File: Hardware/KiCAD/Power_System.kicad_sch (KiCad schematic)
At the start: 0 parts

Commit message: feat: add models, correct hierarchical patterns
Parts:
- added J3: USB_C_Receptacle, Connector_USB:USB_C_Receptacle_GCT_USB4085, symbol Connector:USB_C_Receptacle
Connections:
- new net: J3.A1 (GND), J3.A12 (GND), J3.B1 (GND), J3.B12 (GND)
- new net: J3.A4 (VBUS), J3.A9 (VBUS), J3.B4 (VBUS), J3.B9 (VBUS)
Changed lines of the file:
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@@
 (kicad_sch (version 20230121) (generator eeschema)
   (paper "A4")
+  (symbol (lib_id "Connector:USB_C_Receptacle") (at 46.99 87.63 0) (unit 1)
+    (in_bom yes) (on_board yes) (dnp no) (fields_autoplaced)
+    (property "Reference" "J3" (at 46.99 54.61 0)
+      (effects (font (size 1.27 1.27)))
+    )
+    (property "Value" "USB_C_Receptacle" (at 46.99 57.15 0)
+      (effects (font (size 1.27 1.27)))
+    )
+    (property "Footprint" "Connector_USB:USB_C_Receptacle_GCT_USB4085" (at 50.8 87.63 0)
+      (effects (font (size 1.27 1.27)) hide)
+    )
+    (property "Datasheet" "https://www.usb.org/sites/default/files/documents/usb_type-c.zip" (at 50.8 87.63 0)
+      (effects (font (size 1.27 1.27)) hide)
+    )
+    (pin "A1")
+    (pin "A10")
+    (pin "A11")
+    (pin "A12")
+    (pin "A2")
+    (pin "A3")
+    (pin "A4")
+    (pin "A5")
+    (pin "A6")
+    (pin "A7")
+    (pin "A8")
+    (pin "A9")
+    (pin "B1")
+    (pin "B10")
+    (pin "B11")
+    (pin "B12")
+    (pin "B2")
+    (pin "B3")
+    (pin "B4")
+    (pin "B5")
+    (pin "B6")
+    (pin "B7")
+    (pin "B8")
+    (pin "B9")
+    (pin "S1")
+    (instances
+      (project "Cobalt-Cowboy"
+        (path "/60a68eb1-aa0f-414e-b03b-965ad6b52dab/f41c6f3a-9e23-419e-9eda-91d37d832739"
+          (reference "J3") (unit 1)
+        )
+      )
+    )
+  )
 )

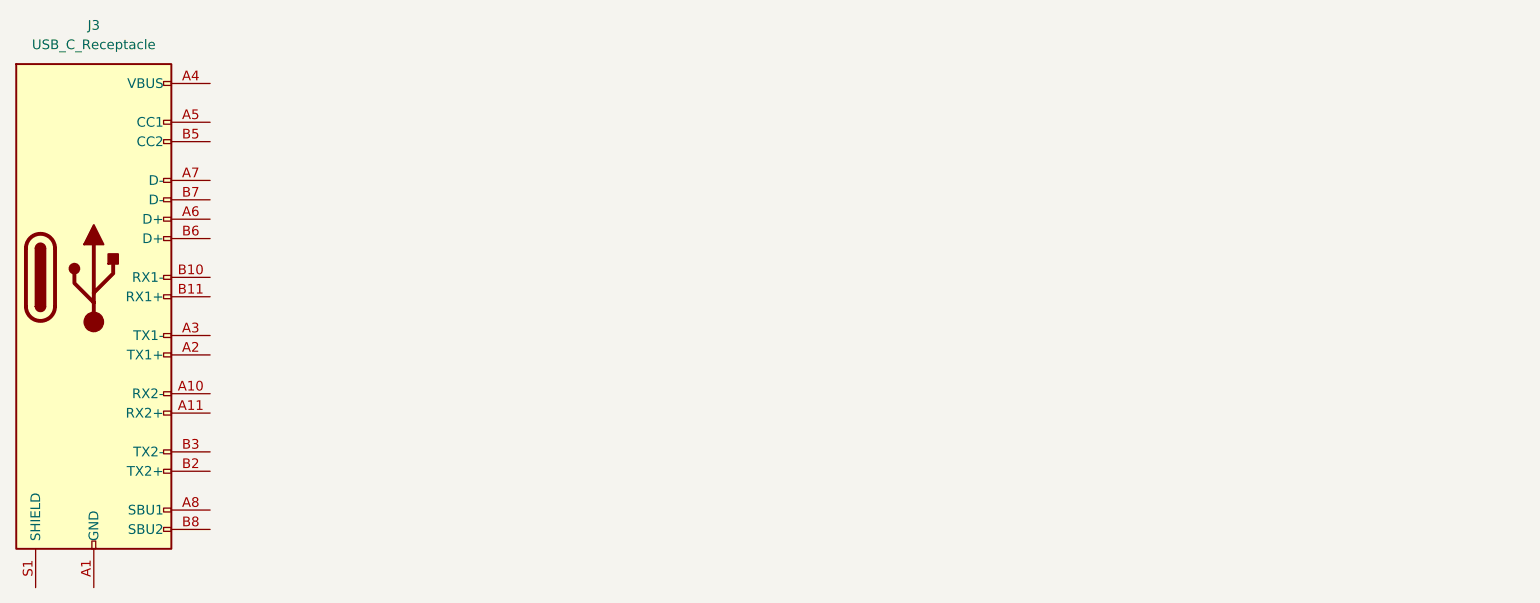
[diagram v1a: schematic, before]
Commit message: added battery to start power systen
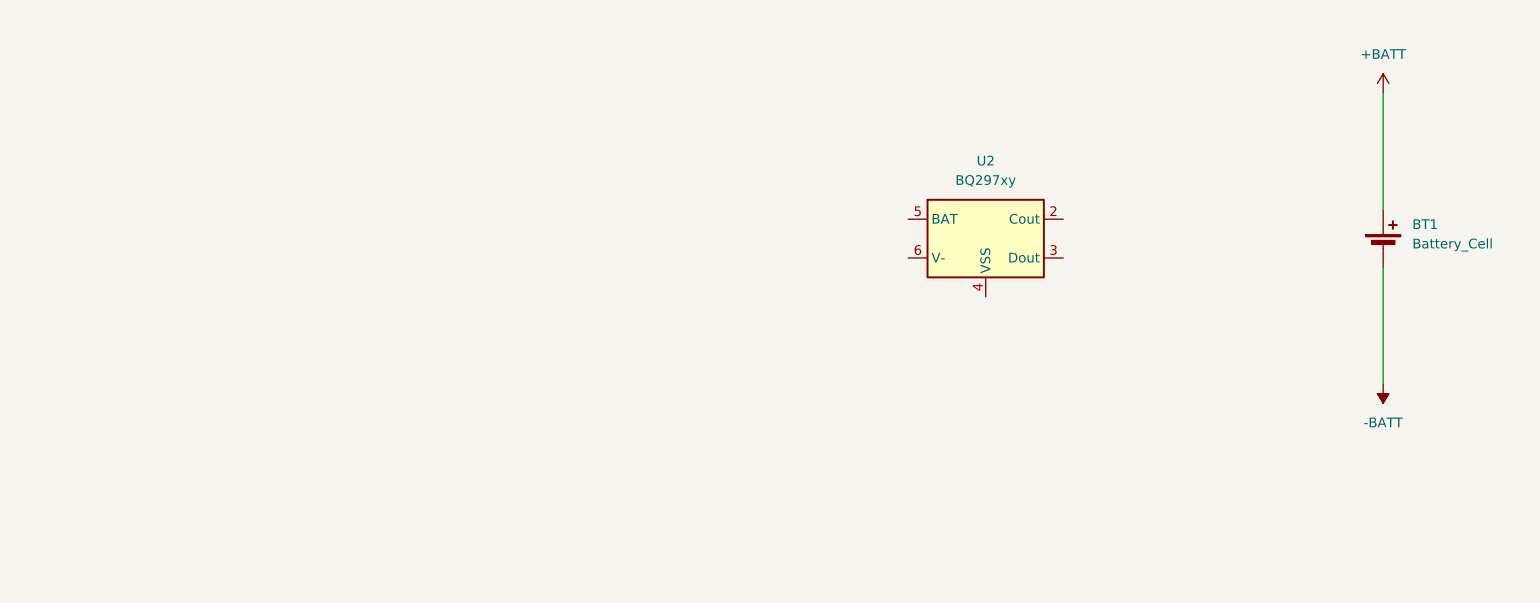
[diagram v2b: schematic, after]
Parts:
- removed J3: USB_C_Receptacle, Connector_USB:USB_C_Receptacle_GCT_USB4085, symbol Connector:USB_C_Receptacle
- added BT1: Battery_Cell, symbol Device:Battery_Cell
- added U2: BQ297xy, Package_SON:WSON-6_1.5x1.5mm_P0.5mm, symbol Battery_Management:BQ297xy
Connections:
- new net +BATT: BT1.1 (+)
- new net -BATT: BT1.2 (-)
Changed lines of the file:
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@@
 (kicad_sch (version 20230121) (generator eeschema)
   (paper "A4")
-  (symbol (lib_id "Connector:USB_C_Receptacle") (at 46.99 87.63 0) (unit 1)
+  (wire (pts (xy 215.9 63.5) (xy 215.9 78.74))
+    (stroke (width 0) (type default))
+  )
+  (wire (pts (xy 215.9 86.36) (xy 215.9 101.6))
+    (stroke (width 0) (type default))
+  )
+  (symbol (lib_id "Device:Battery_Cell") (at 215.9 83.82 0) (unit 1)
     (in_bom yes) (on_board yes) (dnp no) (fields_autoplaced)
-    (property "Reference" "J3" (at 46.99 54.61 0)
-      (effects (font (size 1.27 1.27)))
+    (property "Reference" "BT1" (at 219.71 80.7085 0)
+      (effects (font (size 1.27 1.27)) (justify left))
     )
-    (property "Value" "USB_C_Receptacle" (at 46.99 57.15 0)
-      (effects (font (size 1.27 1.27)))
+    (property "Value" "Battery_Cell" (at 219.71 83.2485 0)
+      (effects (font (size 1.27 1.27)) (justify left))
     )
-    (property "Footprint" "Connector_USB:USB_C_Receptacle_GCT_USB4085" (at 50.8 87.63 0)
+    (property "Footprint" "" (at 215.9 82.296 90)
       (effects (font (size 1.27 1.27)) hide)
     )
-    (property "Datasheet" "https://www.usb.org/sites/default/files/documents/usb_type-c.zip" (at 50.8 87.63 0)
+    (property "Datasheet" "~" (at 215.9 82.296 90)
       (effects (font (size 1.27 1.27)) hide)
     )
-    (pin "A1")
-    (pin "A10")
-    (pin "A11")
-    (pin "A12")
-    (pin "A2")
-    (pin "A3")
-    (pin "A4")
-    (pin "A5")
-    (pin "A6")
-    (pin "A7")
-    (pin "A8")
-    (pin "A9")
-    (pin "B1")
-    (pin "B10")
-    (pin "B11")
-    (pin "B12")
-    (pin "B2")
-    (pin "B3")
-    (pin "B4")
-    (pin "B5")
-    (pin "B6")
-    (pin "B7")
-    (pin "B8")
-    (pin "B9")
-    (pin "S1")
+    (pin "1")
+    (pin "2")
     (instances
       (project "Cobalt-Cowboy"
         (path "/60a68eb1-aa0f-414e-b03b-965ad6b52dab/f41c6f3a-9e23-419e-9eda-91d37d832739"
-          (reference "J3") (unit 1)
+          (reference "BT1") (unit 1)
         )
       )
+    )
+  )
+  (symbol (lib_id "Battery_Management:BQ297xy") (at 163.83 82.55 0) (unit 1)
+    (in_bom yes) (on_board yes) (dnp no) (fields_autoplaced)
+    (property "Reference" "U2" (at 163.83 72.39 0)
+      (effects (font (size 1.27 1.27)))
+    )
+    (property "Value" "BQ297xy" (at 163.83 74.93 0)
+      (effects (font (size 1.27 1.27)))
+    )
+    (property "Footprint" "Package_SON:WSON-6_1.5x1.5mm_P0.5mm" (at 163.83 73.66 0)
+      (effects (font (size 1.27 1.27)) hide)
+    )
+    (property "Datasheet" "http://www.ti.com/lit/ds/symlink/bq2970.pdf" (at 157.48 77.47 0)
+      (effects (font (size 1.27 1.27)) hide)
+    )
+    (pin "1")
+    (pin "2")
+    (pin "3")
+    (pin "4")
+    (pin "5")
+    (pin "6")
+    (instances
+      (project "Cobalt-Cowboy"
+        (path "/60a68eb1-aa0f-414e-b03b-965ad6b52dab/f41c6f3a-9e23-419e-9eda-91d37d832739"
+          (reference "U2") (unit 1)
+        )
+      )
+    )
+  )
+  (symbol (lib_id "power:-BATT") (at 215.9 101.6 180) (unit 1)
+    (in_bom yes) (on_board yes) (dnp no) (fields_autoplaced)
+    (property "Reference" "#PWR039" (at 215.9 97.79 0)
+      (effects (font (size 1.27 1.27)) hide)
+    )
+    (property "Value" "-BATT" (at 215.9 106.68 0)
+      (effects (font (size 1.27 1.27)))
+    )
+    (property "Footprint" "" (at 215.9 101.6 0)
+      (effects (font (size 1.27 1.27)) hide)
+    )
+    (property "Datasheet" "" (at 215.9 101.6 0)
+      (effects (font (size 1.27 1.27)) hide)
+    )
+    (pin "1")
+    (instances
+      (project "Cobalt-Cowboy"
+        (path "/60a68eb1-aa0f-414e-b03b-965ad6b52dab/f41c6f3a-9e23-419e-9eda-91d37d832739"
+          (reference "#PWR039") (unit 1)
+        )
+      )
+    )
+  )
+  (symbol (lib_id "power:+BATT") (at 215.9 63.5 0) (unit 1)
+    (in_bom yes) (on_board yes) (dnp no) (fields_autoplaced)
+    (property "Reference" "#PWR040" (at 215.9 67.31 0)
+      (effects (font (size 1.27 1.27)) hide)
+    )
+    (property "Value" "+BATT" (at 215.9 58.42 0)
+      (effects (font (size 1.27 1.27)))
+    )
+    (property "Footprint" "" (at 215.9 63.5 0)
+      (effects (font (size 1.27 1.27)) hide)
+    )
+    (property "Datasheet" "" (at 215.9 63.5 0)
+      (effects (font (size 1.27 1.27)) hide)
+    )
+    (pin "1")
+    (instances
+      (project "Cobalt-Cowboy"
+        (path "/60a68eb1-aa0f-414e-b03b-965ad6b52dab/f41c6f3a-9e23-419e-9eda-91d37d832739"
+          (reference "#PWR040") (unit 1)
+        )
+      )

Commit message: Added a test for commit
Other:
- note added: "Need to Add USB charging"
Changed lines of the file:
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@@
     (stroke (width 0) (type default))
+  )
+  (text "Need to Add USB charging\n" (at 13.97 16.51 0)
+    (effects (font (size 1.27 1.27)) (justify left bottom))
   )
   (symbol (lib_id "Device:Battery_Cell") (at 215.9 83.82 0) (unit 1)

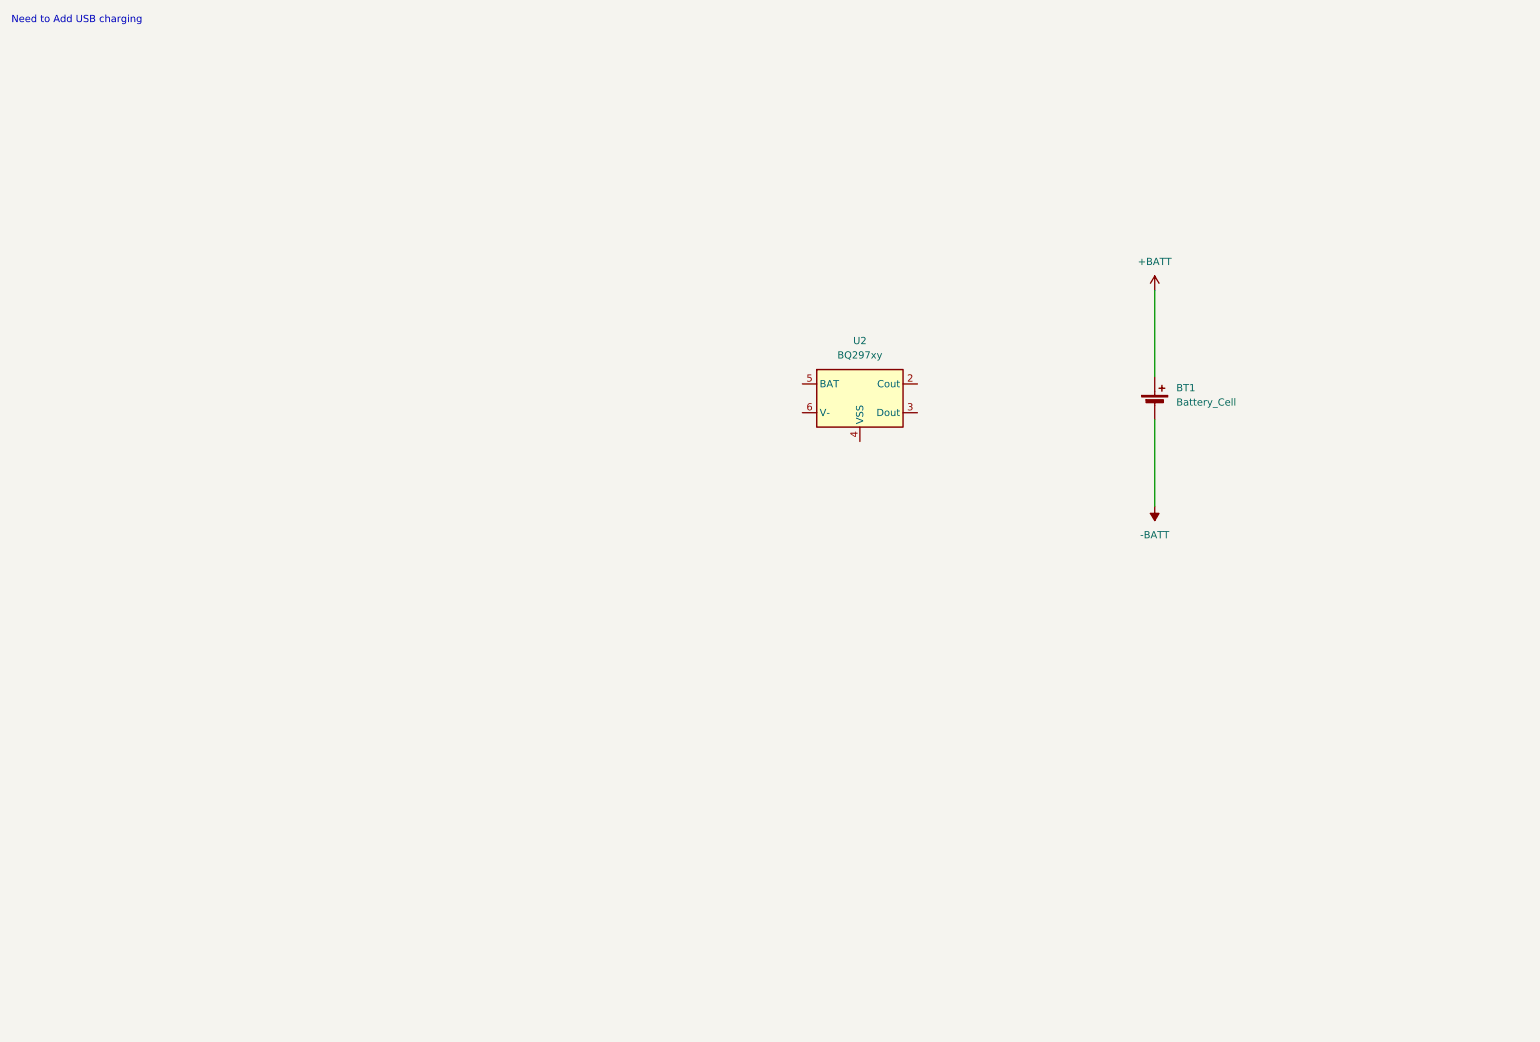
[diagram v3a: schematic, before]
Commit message: feat: corrected Power routing, added TODOs for board, prepared for amps
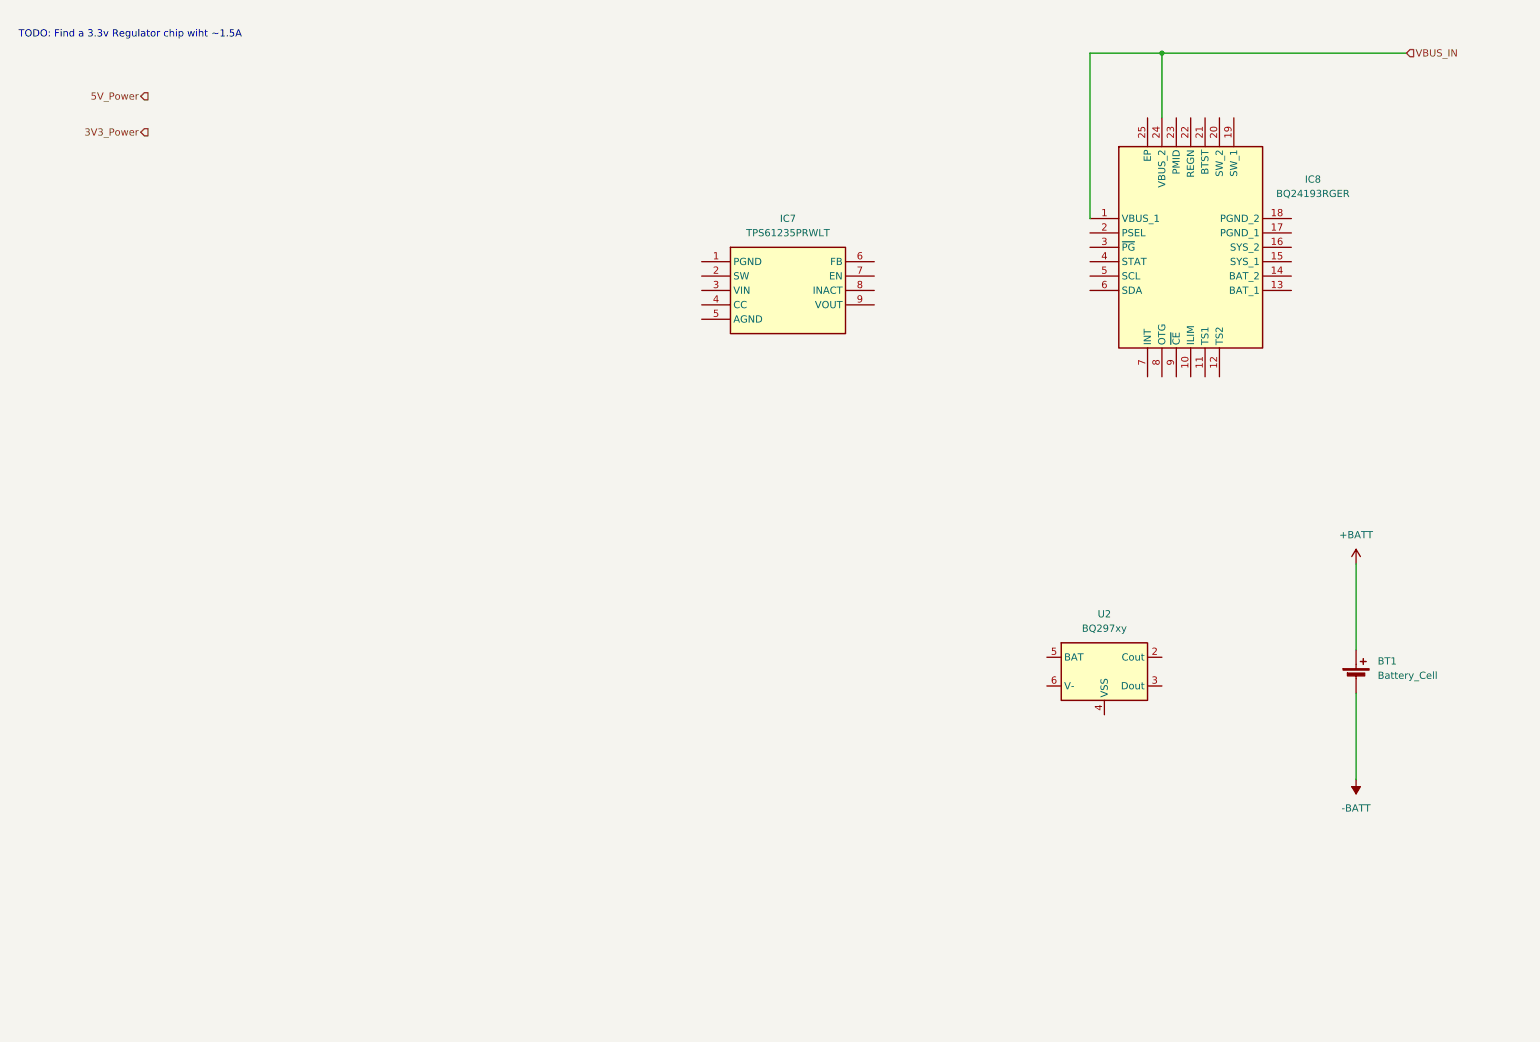
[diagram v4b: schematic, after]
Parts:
- added IC7: TPS61235PRWLT, Cobalt_Cowboy:TPS61235PRWLT, symbol Cobalt-Cowboy:TPS61235PRWLT
- added IC8: BQ24193RGER, Cobalt_Cowboy:QFN50P400X400X100-25N-D_BQ24193RGER, symbol Cobalt-Cowboy:BQ24193RGER
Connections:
- new net VBUS_IN: IC8.1 (VBUS_1), IC8.24 (VBUS_2)
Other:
- note added: "TODO: Find a 3.3v Regulator chip wiht ~1.5A"
- note removed: "Need to Add USB charging"
- moved on the sheet: BT1, U2
